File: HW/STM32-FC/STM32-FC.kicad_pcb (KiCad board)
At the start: 4 copper layers, 39 x 48.5 mm, 131 parts, among them J1 GH 1.25mm 6P, J10 GH 1.25mm 6P, J11 GH 1.25mm 6P, J12 GH 1.25mm 6P, J13 GH 1.25mm 4P, J14 GH 1.25mm 4P, J15 GH 1.25mm 4P, J16 GH 1.25mm 4P, J2 USB_C_USB2.0_14P, J3 GH 1.25mm 6P, J4 TF-06A, J5 JST ZH 1.5mm 2P, J6 PWM_Conn_3x14, J7 ZH 1.5mm 4P, J8 ZH 1.5mm 3P, J9 GH 1.25mm 10P, Q1 PMDPB30XN, Q2 PMDPB30XN, Q3 PMDPB55XP, U1 STM32F407VETx, U10 LPS22HH, U11 TMUX1104, U12 ATA6561-GBQW, U13 ATA6561-GBQW, U2 USBLC6-2SC6, U3 TPS62840, U4 TPS62840, U5 TPS62840, U6 W25X40CLUXIG, U7 BMI323, U8 ICM-42688-P, U9 LIS2MDLTR, Y1 16MHz

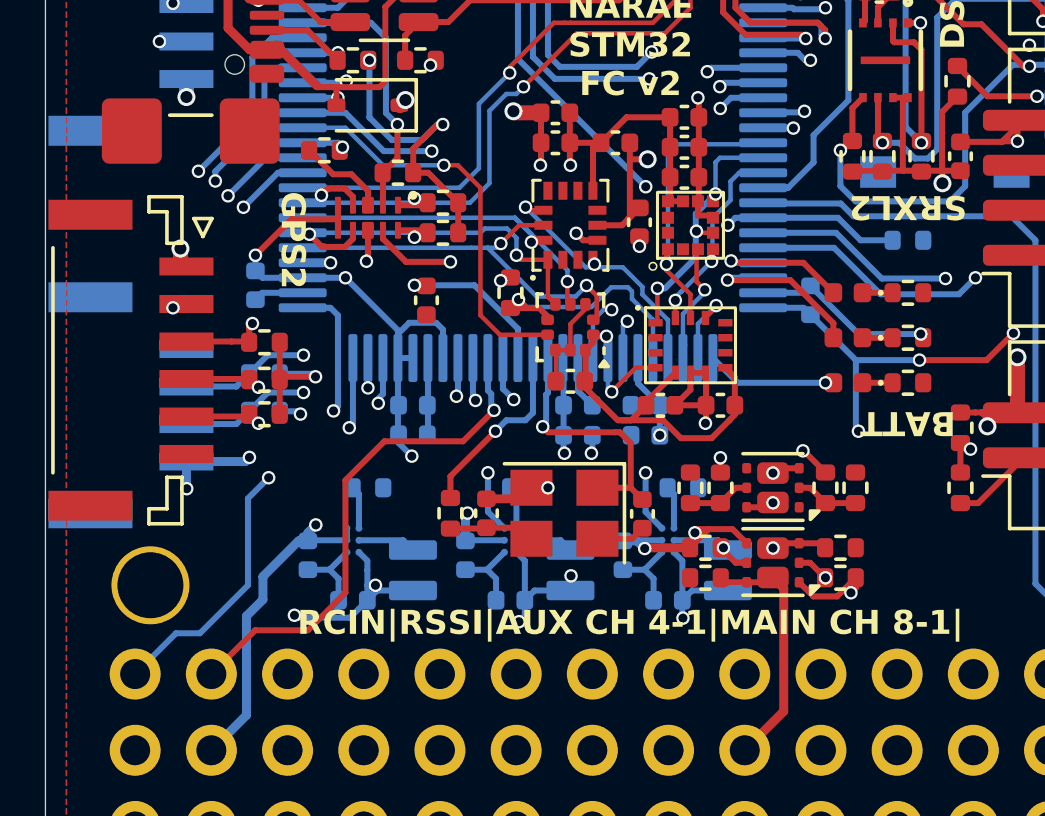
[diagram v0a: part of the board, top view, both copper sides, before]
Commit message: LPS22HH Circuit update
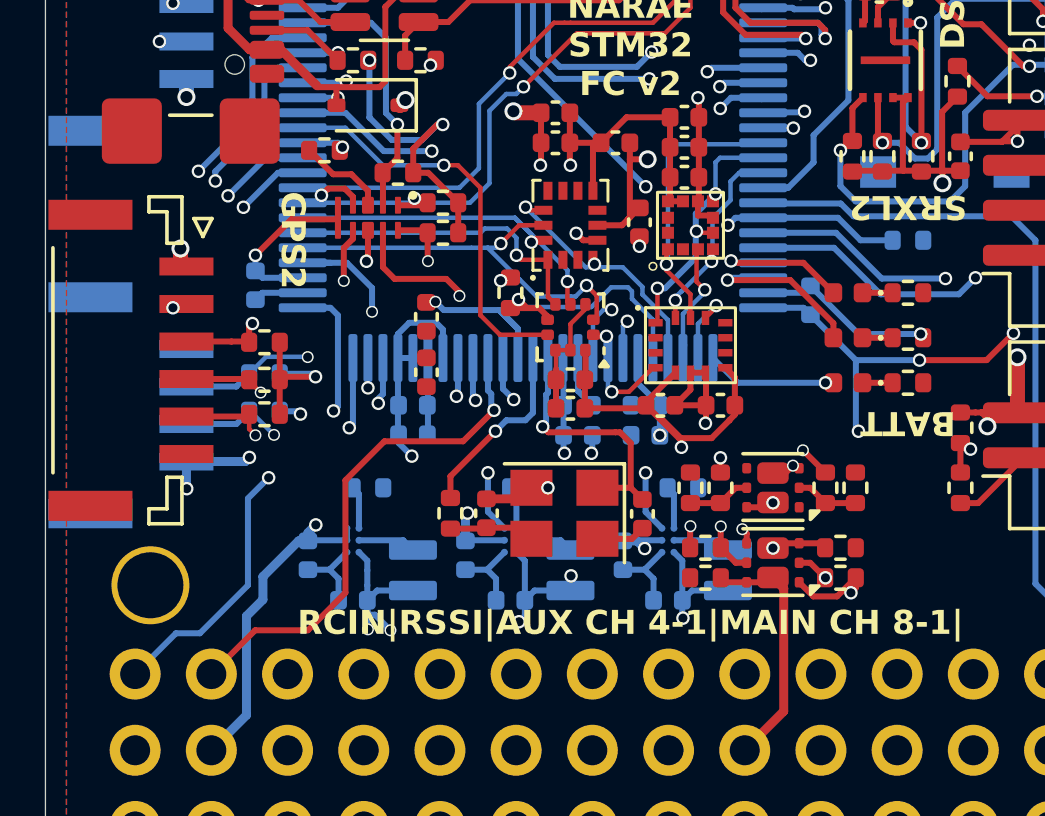
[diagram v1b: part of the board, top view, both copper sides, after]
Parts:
- added C36: 100nF, Capacitor_SMD:C_0402_1005Metric, F.Cu at (137.0, 100.1)
- added C37: 100nF, Capacitor_SMD:C_0402_1005Metric, F.Cu at (132.2, 98.9)
- moved C5 0.55 mm to (132.2, 97.0)
- renumbered J9 to J10, J10 to J11, J11 to J12, J12 to J13, J13 to J14, J14 to J15, J15 to J16, J16 to J8, J8 to J9
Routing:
- net +3.3V: track 93.5 -> 88.4 mm, vias 27 -> 26
- net +5V: track 51.4 -> 48.3 mm, vias 21 -> 22
- net /RC_INPUT/SBUS: track 16.5 -> 19.0 mm
- net /RC_INPUT/RCIN: track 20.7 -> 18.5 mm
- net /RC_SEL1: track 7.91 -> 10.0 mm
- net Net-(Q3B-G): track 5.19 -> 7.13 mm
- net /RC_TX: track 65.4 -> 67.2 mm
- net GND: track 85.6 -> 86.9 mm
- net /I2C2_SDA: track 18.7 -> 20.0 mm
- net /SW_PWR_RC: track 18.3 -> 19.4 mm
- net /I2C1_SCL: track 33.8 -> 34.7 mm
- net /I2C2_SCL: track 16.6 -> 17.4 mm
- net /NRST: track 23.3 -> 23.8 mm
- net +3.3VA: track 49.9 -> 50.1 mm, vias 6 -> 7
